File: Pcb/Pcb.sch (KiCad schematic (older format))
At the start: 134 parts, among them J1 TRRS, J2 JST, Q1 2N7002, SW1 SW_Push, SW10 SW_Push, SW11 SW_Push, SW12 SW_Push, SW13 SW_Push, SW14 SW_Push, SW15 SW_Push, SW16 SW_Push, SW17 SW_Push, SW18 SW_Push, SW19 SW_Push, SW2 SW2, SW20 SW_Push, SW21 SW_Push, SW22 SW_Push, SW23 SW_Push, SW24 SW_Push, SW25 SW_Push, SW26 SW_Push, SW27 SW_Push, SW28 SW_Push, SW29 SW_Push, SW3 SW_Push, SW4 SW_Push, SW5 SW_Push, SW6 SW_Push, SW7 SW_Push, SW8 SW_Push, SW9 SW_Push, U1 ProMicro

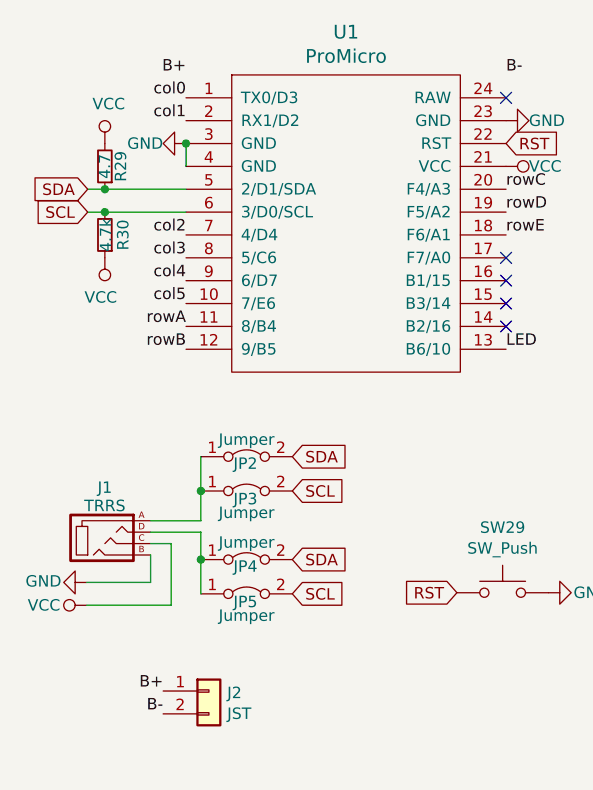
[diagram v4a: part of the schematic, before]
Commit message: Remove I2C resistors
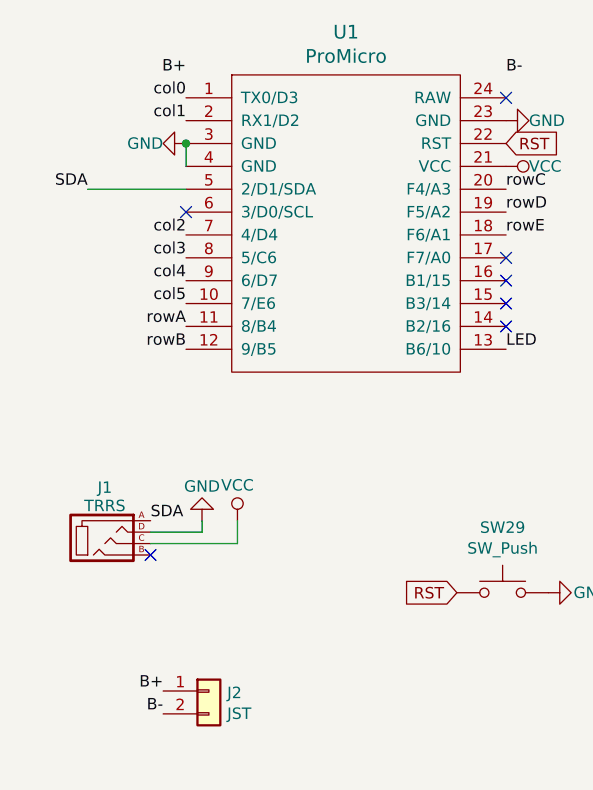
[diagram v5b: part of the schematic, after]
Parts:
- removed JP2, JP3, JP4, JP5: Jumper, 1symblos:Jumper, symbol Jumper:Jumper_2_Bridged
- removed R29: 4.7, Used_Footprints:Resistor_Hybrid_1205, symbol Device:R_Small
- removed R30: 4.7k, Used_Footprints:Resistor_Hybrid_1205, symbol Device:R_Small
- J2: footprint (none) -> Used_Footprints:JST_THT_2.0
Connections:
- net GND: now also J1.D; no longer J1.B
- net SDA: now also J1.A
- net SCL: no longer names the net of U1.6 (3/D0/SCL)
- no-connect marks 5 -> 7
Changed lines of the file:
@@
 Text Label 1240 1045 2    50   ~ 0
 col1
-$Comp
-L Device:R_Small R29
-U 1 1 5DAAA6F2
-P 885 1245
-F 0 "R29" V 815 1245 50  0000 C CNN
-F 1 "4.7" V 885 1245 50  0000 C CNN
-F 2 "Used_Footprints:Resistor_Hybrid_1205" H 885 1245 50  0001 C CNN
-F 3 "~" H 885 1245 50  0001 C CNN
-	1    885  1245
-	-1   0    0    1
-$EndComp
-$Comp
-L Device:R_Small R30
-U 1 1 5DAAB292
-P 885 1545
-F 0 "R30" V 805 1545 50  0000 C CNN
-F 1 "4.7k" V 880 1545 50  0000 C CNN
-F 2 "Used_Footprints:Resistor_Hybrid_1205" H 885 1545 50  0001 C CNN
-F 3 "~" H 885 1545 50  0001 C CNN
-	1    885  1545
-	-1   0    0    1
-$EndComp
-Text GLabel 810  1345 0    50   Input ~ 0
-SDA
-Text GLabel 810  1445 0    50   Input ~ 0
-SCL
 Text Label 1240 1545 2    50   ~ 0
 col2
@@
 Text GLabel 2640 1145 2    50   Input ~ 0
 RST
-Wire Wire Line
-	810  1345 885  1345
-Wire Wire Line
-	810  1445 885  1445
-Connection ~ 885  1445
-Wire Wire Line
-	885  1445 1240 1445
-Connection ~ 885  1345
-Wire Wire Line
-	885  1345 1240 1345
-$Comp
-L power:VCC #PWR0101
-U 1 1 5DBF6680
-P 885 1145
-F 0 "#PWR0101" H 885 995 50  0001 C CNN
-F 1 "VCC" H 902 1318 50  0000 C CNN
-F 2 "" H 885 1145 50  0001 C CNN
-F 3 "" H 885 1145 50  0001 C CNN
-	1    885  1145
-	1    0    0    -1
-$EndComp
-$Comp
-L power:VCC #PWR0102
-U 1 1 5DBF75FF
-P 885 1645
-F 0 "#PWR0102" H 885 1495 50  0001 C CNN
-F 1 "VCC" H 903 1818 50  0000 C CNN
-F 2 "" H 885 1645 50  0001 C CNN
-F 3 "" H 885 1645 50  0001 C CNN
-	1    885  1645
-	-1   0    0    1
-$EndComp
-$Comp
-L power:GND #PWR0106
-U 1 1 5DC1A713
-P 805 3065
-F 0 "#PWR0106" H 805 2815 50  0001 C CNN
-F 1 "GND" V 800 2955 50  0000 R CNN
-F 2 "" H 805 3065 50  0001 C CNN
-F 3 "" H 805 3065 50  0001 C CNN
-	1    805  3065
-	0    1    1    0
-$EndComp
-$Comp
-L power:VCC #PWR0107
-U 1 1 5DC1BBEB
-P 805 3165
-F 0 "#PWR0107" H 805 3015 50  0001 C CNN
-F 1 "VCC" V 805 3280 50  0000 L CNN
-F 2 "" H 805 3165 50  0001 C CNN
-F 3 "" H 805 3165 50  0001 C CNN
-	1    805  3165
-	0    -1   -1   0
-$EndComp
-Wire Wire Line
-	1085 2945 1085 3065
-Wire Wire Line
-	1085 3065 805  3065
-Wire Wire Line
-	1085 2895 1175 2895
-Wire Wire Line
-	1175 2895 1175 3165
-Wire Wire Line
-	1175 3165 805  3165
-$Comp
-L Jumper:Jumper_2_Bridged JP4
-U 1 1 5DC2DEC8
-P 1505 2965
-F 0 "JP4" H 1500 2935 50  0000 C CNN
-F 1 "Jumper" H 1505 3040 50  0000 C CNN
-F 2 "1symblos:Jumper" H 1505 2965 50  0001 C CNN
-F 3 "~" H 1505 2965 50  0001 C CNN
-	1    1505 2965
-	1    0    0    -1
-$EndComp
-$Comp
-L Jumper:Jumper_2_Bridged JP5
-U 1 1 5DC322E4
-P 1505 3115
-F 0 "JP5" H 1500 3080 50  0000 C CNN
-F 1 "Jumper" H 1505 3020 50  0000 C CNN
-F 2 "1symblos:Jumper" H 1505 3115 50  0001 C CNN
-F 3 "~" H 1505 3115 50  0001 C CNN
-	1    1505 3115
-	1    0    0    -1
-$EndComp
-$Comp
-L Jumper:Jumper_2_Bridged JP2
-U 1 1 5DC382C2
-P 1505 2515
-F 0 "JP2" H 1500 2485 50  0000 C CNN
-F 1 "Jumper" H 1505 2590 50  0000 C CNN
-F 2 "1symblos:Jumper" H 1505 2515 50  0001 C CNN
-F 3 "~" H 1505 2515 50  0001 C CNN
-	1    1505 2515
-	1    0    0    -1
-$EndComp
-$Comp
-L Jumper:Jumper_2_Bridged JP3
-U 1 1 5DC382C8
-P 1505 2665
-F 0 "JP3" H 1500 2630 50  0000 C CNN
-F 1 "Jumper" H 1505 2570 50  0000 C CNN
-F 2 "1symblos:Jumper" H 1505 2665 50  0001 C CNN
-F 3 "~" H 1505 2665 50  0001 C CNN
-	1    1505 2665
-	1    0    0    -1
-$EndComp
-Wire Wire Line
-	1085 2845 1305 2845
-Wire Wire Line
-	1305 2845 1305 2965
-Connection ~ 1305 2965
-Wire Wire Line
-	1305 2965 1305 3115
-Wire Wire Line
-	1085 2795 1305 2795
-Wire Wire Line
-	1305 2795 1305 2665
-Connection ~ 1305 2665
-Wire Wire Line
-	1305 2665 1305 2515
-Text GLabel 1705 2515 2    50   Input ~ 0
-SDA
-Text GLabel 1705 2665 2    50   Input ~ 0
-SCL
-Text GLabel 1705 2965 2    50   Input ~ 0
-SDA
-Text GLabel 1705 3115 2    50   Input ~ 0
-SCL
 $Comp
 L Mechanical:MountingHole HM1
@@
 F 0 "J2" H 1420 3532 50  0000 L CNN
 F 1 "JST" H 1420 3441 50  0000 L CNN
-F 2 "" H 1340 3540 50  0001 C CNN
+F 2 "Used_Footprints:JST_THT_2.0" H 1340 3540 50  0001 C CNN
 F 3 "~" H 1340 3540 50  0001 C CNN
 	1    1340 3540
@@
 Text Label 1140 3640 2    50   ~ 0
 B-
+Wire Wire Line
+	810  1345 1240 1345
+NoConn ~ 1240 1445
+Text Label 810  1345 2    50   ~ 0
+SDA
+Text Label 1085 2795 0    50   ~ 0
+SDA
+$Comp
+L power:GND #PWR?
+U 1 1 5E5516DF
+P 1310 2795
+F 0 "#PWR?" H 1310 2545 50  0001 C CNN
+F 1 "GND" H 1310 2645 50  0000 C CNN
+F 2 "" H 1310 2795 50  0001 C CNN
+F 3 "" H 1310 2795 50  0001 C CNN
+	1    1310 2795
+	-1   0    0    1
+$EndComp
+Wire Wire Line
+	1085 2845 1310 2845
+Wire Wire Line
+	1310 2845 1310 2795
+$Comp
+L power:VCC #PWR?
+U 1 1 5E557C13
+P 1465 2795
+F 0 "#PWR?" H 1465 2645 50  0001 C CNN
+F 1 "VCC" H 1465 2950 50  0000 C CNN
+F 2 "" H 1465 2795 50  0001 C CNN
+F 3 "" H 1465 2795 50  0001 C CNN
+	1    1465 2795
+	1    0    0    -1
+$EndComp
+Wire Wire Line
+	1465 2795 1465 2895
+Wire Wire Line
+	1465 2895 1085 2895
+NoConn ~ 1085 2945
 $EndSCHEMATC

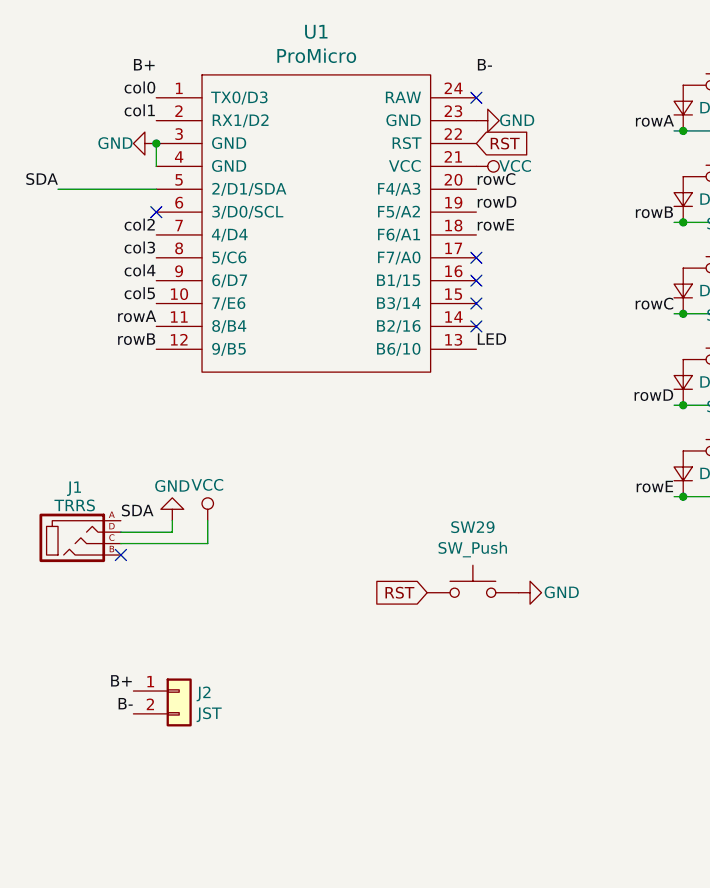
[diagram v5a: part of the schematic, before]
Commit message: Remove JST connector from scheme
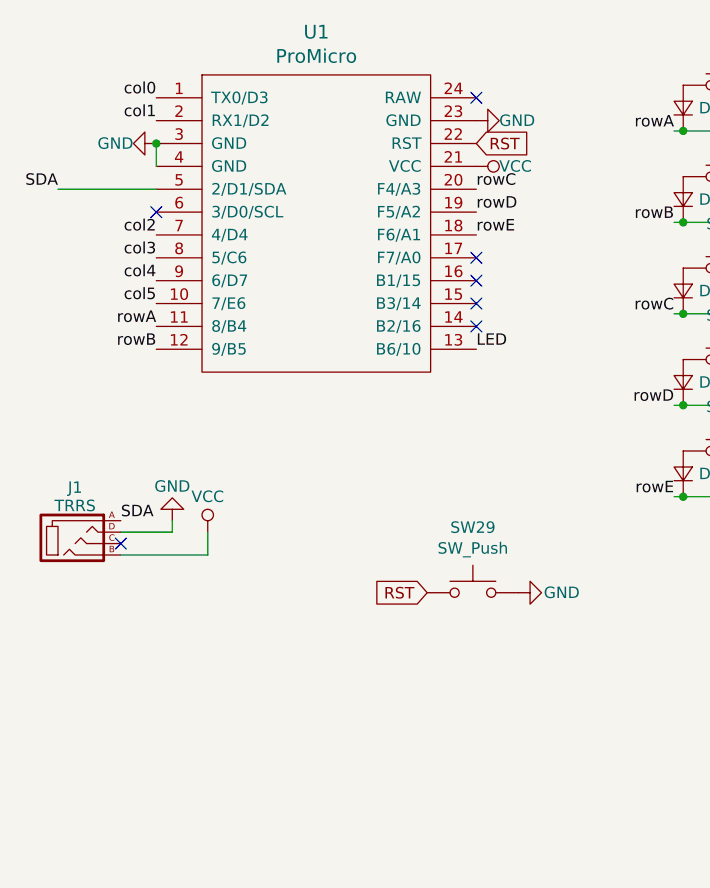
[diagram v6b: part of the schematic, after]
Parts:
- removed J2: JST, Used_Footprints:JST_THT_2.0, symbol Connector_Generic:Conn_01x02
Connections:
- net VCC: now also J1.B; no longer J1.C
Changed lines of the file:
@@
 Comment4 ""
 $EndDescr
-$Comp
-L kbd:ProMicro U1
-U 1 1 5DAA926E
-P 1940 1695
-F 0 "U1" H 1940 2732 60  0000 C CNN
-F 1 "ProMicro" H 1940 2626 60  0000 C CNN
-F 2 "Used_Footprints:ProMicro_Dual" H 2040 645 60  0001 C CNN
-F 3 "" H 2040 645 60  0000 C CNN
-	1    1940 1695
-	1    0    0    -1
-$EndComp
 NoConn ~ 2640 945
 NoConn ~ 2640 1645
@@
 Wire Wire Line
 	1240 1245 1240 1145
-Connection ~ 1240 1145
 $Comp
 L Switch:SW_Push SW1
@@
 NoConn ~ 2640 1845
 NoConn ~ 2640 1745
-Text Label 1240 845  2    50   ~ 0
-B+
-Text Label 2640 845  0    50   ~ 0
-B-
-$Comp
-L Connector_Generic:Conn_01x02 J2
-U 1 1 5E57C502
-P 1340 3540
-F 0 "J2" H 1420 3532 50  0000 L CNN
-F 1 "JST" H 1420 3441 50  0000 L CNN
-F 2 "Used_Footprints:JST_THT_2.0" H 1340 3540 50  0001 C CNN
-F 3 "~" H 1340 3540 50  0001 C CNN
-	1    1340 3540
-	1    0    0    -1
-$EndComp
-Text Label 1140 3540 2    50   ~ 0
-B+
-Text Label 1140 3640 2    50   ~ 0
-B-
 Wire Wire Line
 	810  1345 1240 1345
@@
 SDA
 $Comp
-L power:GND #PWR?
+L power:GND #PWR0101
 U 1 1 5E5516DF
 P 1310 2795
-F 0 "#PWR?" H 1310 2545 50  0001 C CNN
+F 0 "#PWR0101" H 1310 2545 50  0001 C CNN
 F 1 "GND" H 1310 2645 50  0000 C CNN
 F 2 "" H 1310 2795 50  0001 C CNN
@@
 	1310 2845 1310 2795
 $Comp
-L power:VCC #PWR?
+L power:VCC #PWR0102
 U 1 1 5E557C13
-P 1465 2795
-F 0 "#PWR?" H 1465 2645 50  0001 C CNN
-F 1 "VCC" H 1465 2950 50  0000 C CNN
-F 2 "" H 1465 2795 50  0001 C CNN
-F 3 "" H 1465 2795 50  0001 C CNN
-	1    1465 2795
-	1    0    0    -1
-$EndComp
-Wire Wire Line
-	1465 2795 1465 2895
-Wire Wire Line
-	1465 2895 1085 2895
-NoConn ~ 1085 2945
+P 1465 2845
+F 0 "#PWR0102" H 1465 2695 50  0001 C CNN
+F 1 "VCC" H 1465 3000 50  0000 C CNN
+F 2 "" H 1465 2845 50  0001 C CNN
+F 3 "" H 1465 2845 50  0001 C CNN
+	1    1465 2845
+	1    0    0    -1
+$EndComp
+Wire Wire Line
+	1465 2845 1465 2945
+Wire Wire Line
+	1465 2945 1085 2945
+NoConn ~ 1085 2895
+Connection ~ 1240 1145
+$Comp
+L kbd:ProMicro U1
+U 1 1 5DAA926E
+P 1940 1695
+F 0 "U1" H 1940 2732 60  0000 C CNN
+F 1 "ProMicro" H 1940 2626 60  0000 C CNN
+F 2 "Used_Footprints:ProMicro_Dual" H 2040 645 60  0001 C CNN
+F 3 "" H 2040 645 60  0000 C CNN
+	1    1940 1695
+	1    0    0    -1
+$EndComp
 $EndSCHEMATC

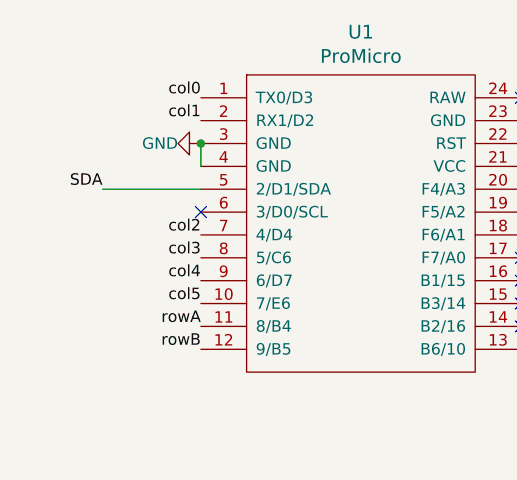
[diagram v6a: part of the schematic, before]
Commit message: Add label for SCL
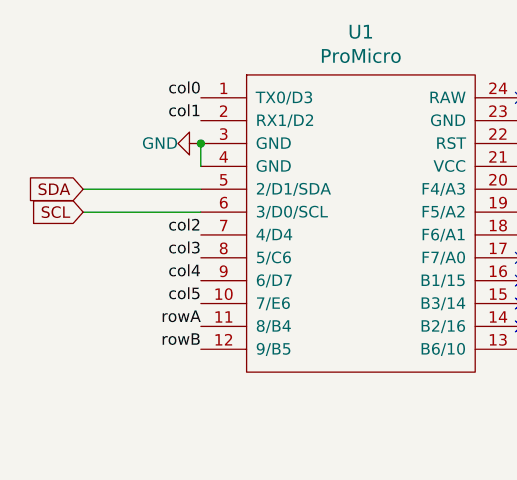
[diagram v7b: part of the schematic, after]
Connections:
- net SCL: now reaches U1.6 (3/D0/SCL)
- no-connect marks 7 -> 6
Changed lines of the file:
@@
 NoConn ~ 2640 1845
 NoConn ~ 2640 1745
-Wire Wire Line
-	810  1345 1240 1345
-NoConn ~ 1240 1445
-Text Label 810  1345 2    50   ~ 0
-SDA
 Text Label 1085 2795 0    50   ~ 0
 SDA
@@
 	1    0    0    -1
 $EndComp
+Text GLabel 725  1345 0    50   Input ~ 0
+SDA
+Text GLabel 725  1445 0    50   Input ~ 0
+SCL
+Wire Wire Line
+	725  1345 1240 1345
+Wire Wire Line
+	725  1445 1240 1445
 $EndSCHEMATC

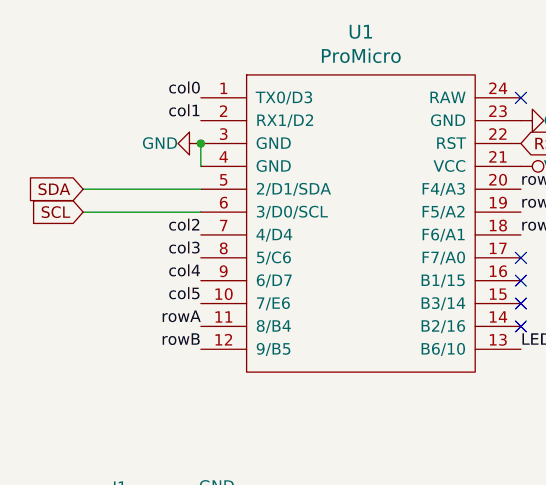
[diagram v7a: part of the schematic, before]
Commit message: Add 4.7k resistor for I2C
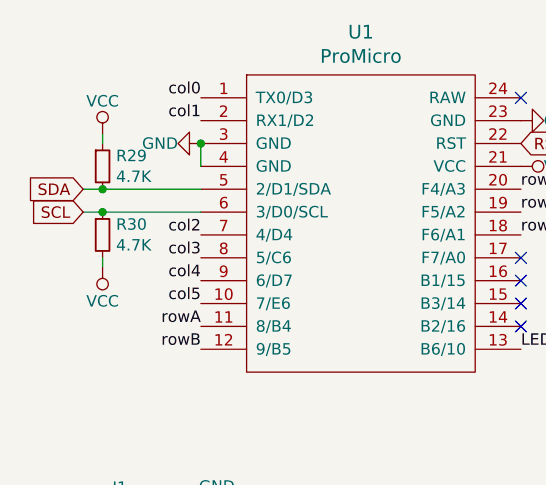
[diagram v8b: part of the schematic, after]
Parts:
- added R29, R30: 4.7K, symbol Device:R_Small
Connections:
- net SCL: now also R30.1
- net SDA: now also R29.2
- net VCC: now also R29.1, R30.2
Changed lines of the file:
@@
 SCL
 Wire Wire Line
-	725  1345 1240 1345
+	725  1345 810  1345
+$Comp
+L Device:R_Small R29
+U 1 1 5E5A5774
+P 810 1245
+F 0 "R29" H 869 1291 50  0000 L CNN
+F 1 "4.7K" H 869 1200 50  0000 L CNN
+F 2 "" H 810 1245 50  0001 C CNN
+F 3 "~" H 810 1245 50  0001 C CNN
+	1    810  1245
+	1    0    0    -1
+$EndComp
+Connection ~ 810  1345
 Wire Wire Line
-	725  1445 1240 1445
+	810  1345 1240 1345
+$Comp
+L Device:R_Small R30
+U 1 1 5E5A67AE
+P 810 1545
+F 0 "R30" H 869 1591 50  0000 L CNN
+F 1 "4.7K" H 869 1500 50  0000 L CNN
+F 2 "" H 810 1545 50  0001 C CNN
+F 3 "~" H 810 1545 50  0001 C CNN
+	1    810  1545
+	1    0    0    -1
+$EndComp
+Wire Wire Line
+	725  1445 810  1445
+Connection ~ 810  1445
+Wire Wire Line
+	810  1445 1240 1445
+$Comp
+L power:VCC #PWR?
+U 1 1 5E5BBB5F
+P 810 1105
+F 0 "#PWR?" H 810 955 50  0001 C CNN
+F 1 "VCC" H 810 1250 50  0000 C CNN
+F 2 "" H 810 1105 50  0001 C CNN
+F 3 "" H 810 1105 50  0001 C CNN
+	1    810  1105
+	1    0    0    -1
+$EndComp
+$Comp
+L power:VCC #PWR?
+U 1 1 5E5BC852
+P 810 1685
+F 0 "#PWR?" H 810 1535 50  0001 C CNN
+F 1 "VCC" H 810 1835 50  0000 C CNN
+F 2 "" H 810 1685 50  0001 C CNN
+F 3 "" H 810 1685 50  0001 C CNN
+	1    810  1685
+	-1   0    0    1
+$EndComp
+Wire Wire Line
+	810  1685 810  1645
+Wire Wire Line
+	810  1105 810  1145
 $EndSCHEMATC
